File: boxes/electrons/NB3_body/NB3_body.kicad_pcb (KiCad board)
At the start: 2 copper layers, 200 x 199.5 mm, 36 parts, among them J1 Conn_02x05_Counter_Clockwise, J10 Conn_02x03_Top_Bottom, J11 Conn_02x03_Top_Bottom, J12 Conn_02x03_Top_Bottom, J13 JST ZH 6-way Socket, J14 JST ZH 6-way Socket, J2 Conn_02x05_Counter_Clockwise, J3 Conn_02x05_Counter_Clockwise, J4 Conn_02x05_Counter_Clockwise, J5 Conn_02x05_Counter_Clockwise, J6 Conn_02x05_Counter_Clockwise, J7 Conn_02x05_Counter_Clockwise, J8 Conn_02x05_Counter_Clockwise, J9 JST SH 4-way Socket

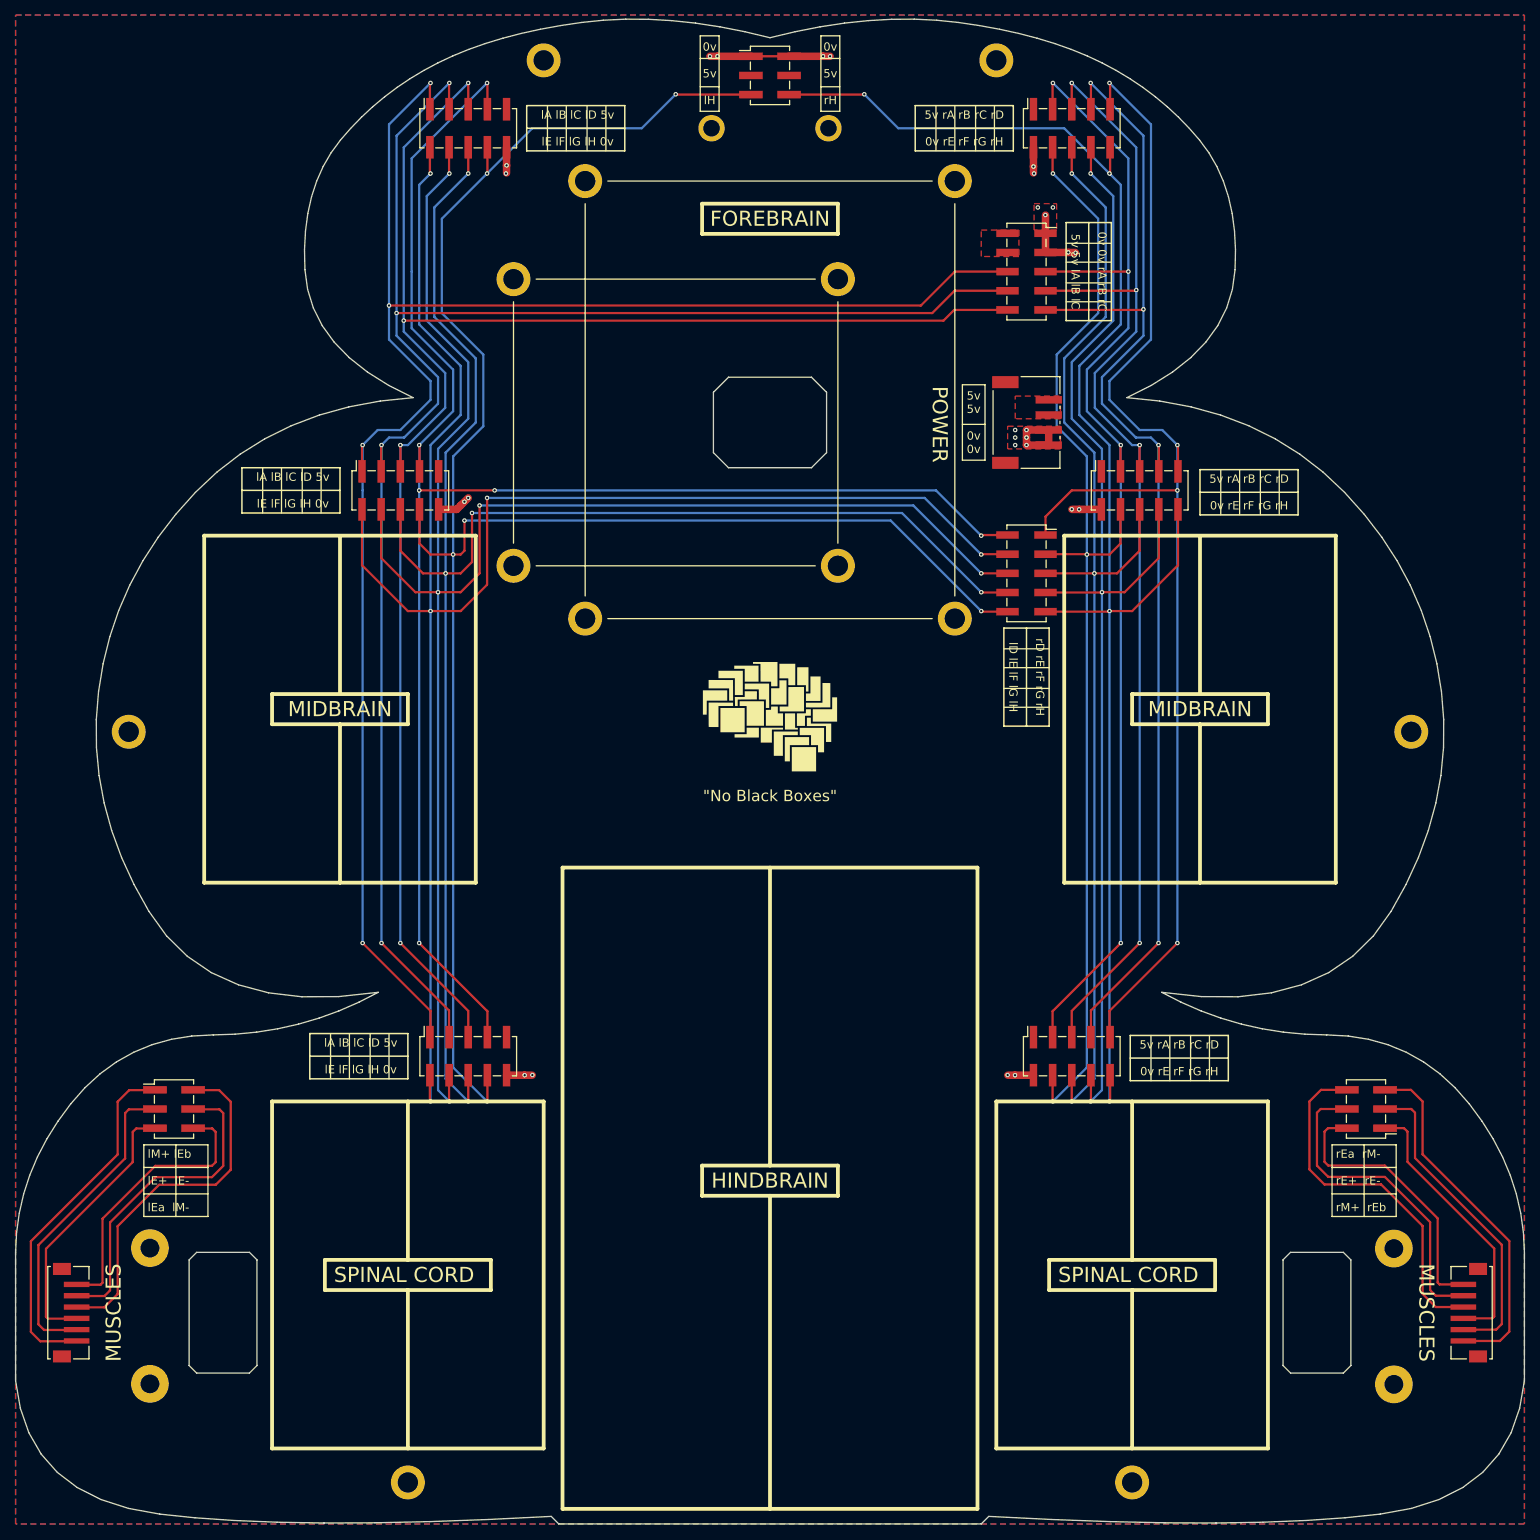
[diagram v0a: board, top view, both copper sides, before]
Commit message: Update NB3_body (motor mount holes)
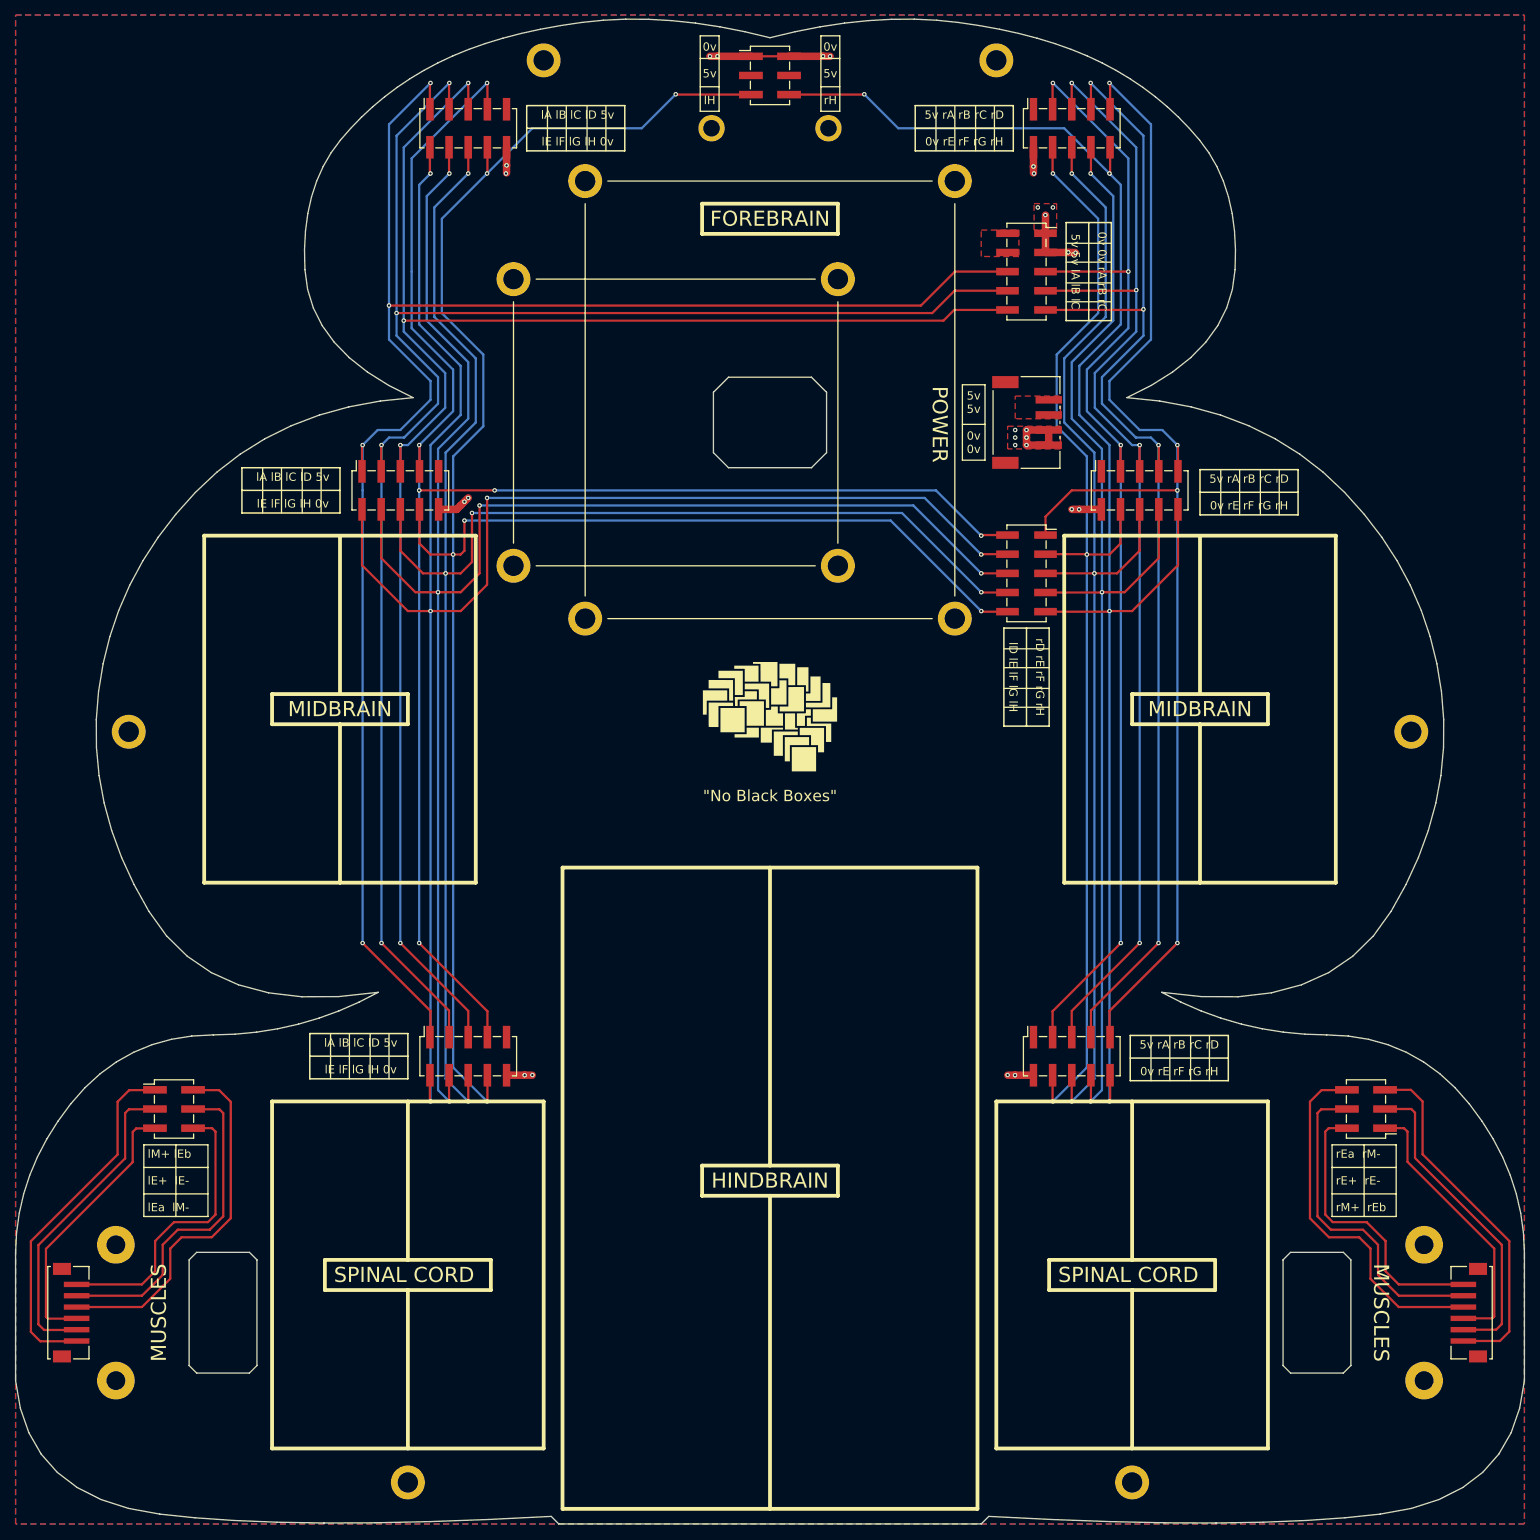
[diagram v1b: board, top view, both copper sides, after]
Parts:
- moved H11 4.53 mm to (37.8, 204.0)
- moved H9 4.53 mm to (37.8, 186.0)
- moved H10 4.03 mm to (211.2, 186.0)
- moved H12 4.03 mm to (211.2, 204.0)
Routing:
- net /LM-: track 37.3 -> 38.7 mm
- net /RM+: track 37.3 -> 38.7 mm
- net /RE+: track 43.0 -> 44.0 mm
- net /LE-: track 43.0 -> 44.0 mm
- net /RE A: track 47.8 -> 48.7 mm
- net /LE B: track 47.8 -> 48.7 mm
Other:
- board text added: "NB3_body Rev 0.0.2"
- board text removed: "NB3_body Rev 0.0.1"

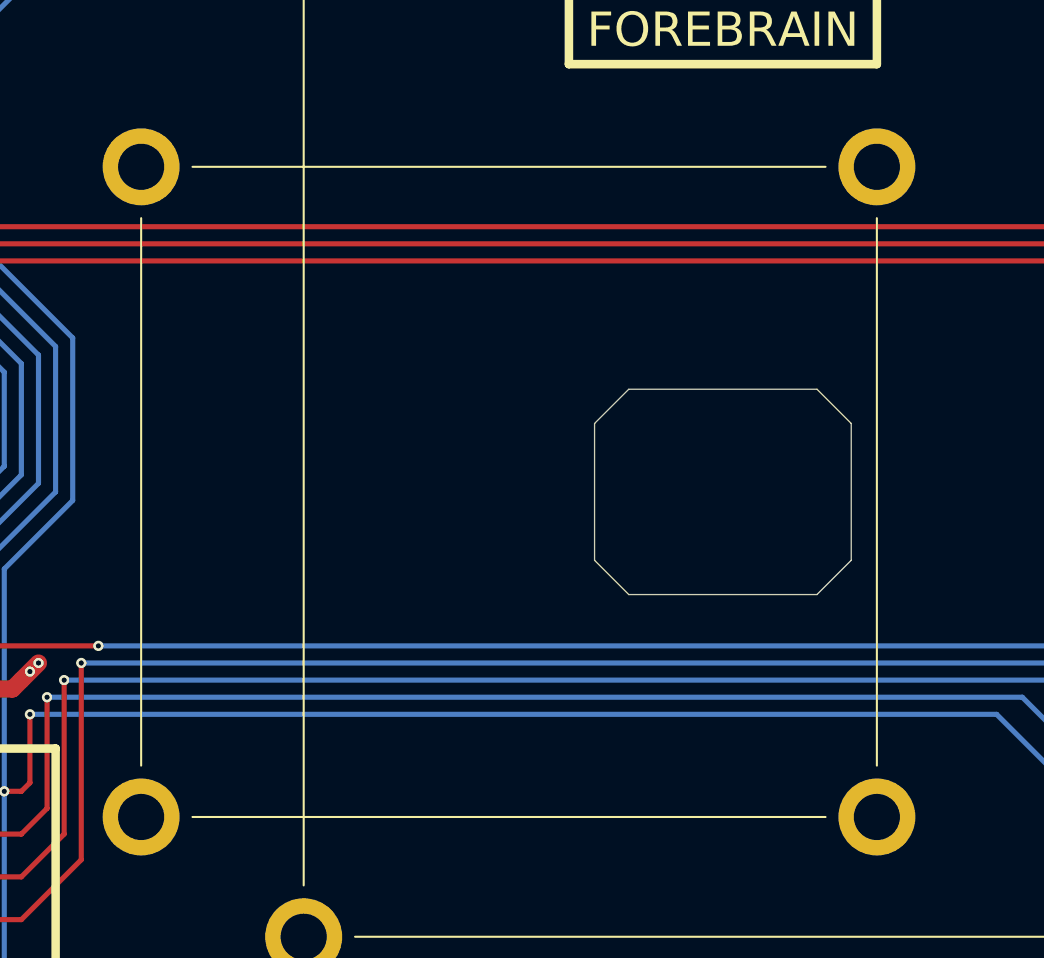
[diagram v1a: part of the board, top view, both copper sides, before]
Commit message: Update NB3_body: new power dimensions
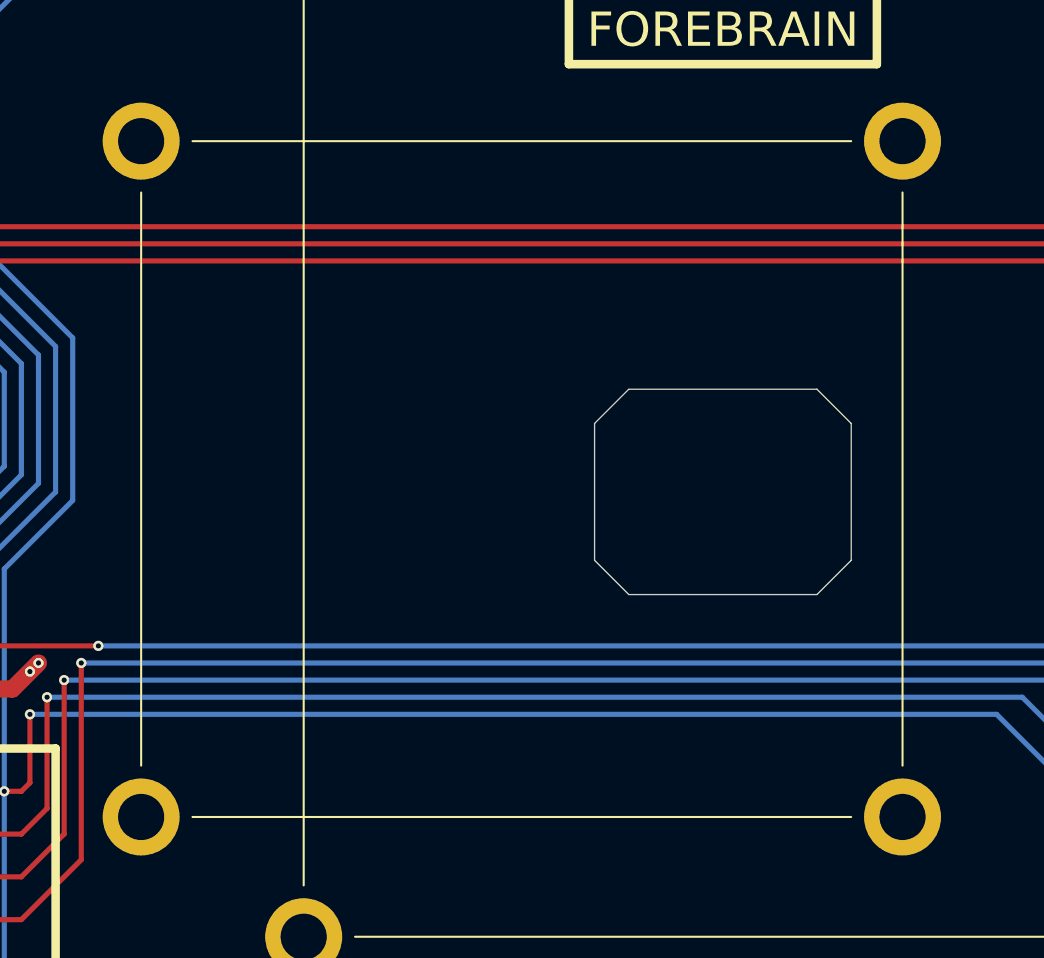
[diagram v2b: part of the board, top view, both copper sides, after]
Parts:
- moved H2 2.12 mm to (135.0, 56.5)
- moved H1 1.50 mm to (90.5, 56.5)
- moved H4 1.50 mm to (135.0, 96.0)
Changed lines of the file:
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@@
   )
   (footprint "MountingHole:MountingHole_2.7mm_M2.5_ISO7380_Pad" (layer "F.Cu")
-    (at 133.5 58)
+    (at 135 56.5)
     (descr "Mounting Hole 2.7mm, M2.5, ISO7380")
     (tags "mounting hole 2.7mm m2.5 iso7380")
@@
   )
   (footprint "MountingHole:MountingHole_2.7mm_M2.5_ISO7380_Pad" (layer "F.Cu")
-    (at 133.5 96)
+    (at 135 96)
     (descr "Mounting Hole 2.7mm, M2.5, ISO7380")
     (tags "mounting hole 2.7mm m2.5 iso7380")
@@
   )
   (footprint "MountingHole:MountingHole_2.7mm_M2.5_ISO7380_Pad" (layer "F.Cu")
-    (at 90.5 58)
+    (at 90.5 56.5)
     (descr "Mounting Hole 2.7mm, M2.5, ISO7380")
     (tags "mounting hole 2.7mm m2.5 iso7380")
@@
   (gr_line (start 68.75 158) (end 68.75 164) (layer "F.SilkS") (width 0.12))
   (gr_line (start 65 83) (end 65 89) (layer "F.SilkS") (width 0.12))
-  (gr_line (start 133.5 61) (end 133.5 93) (layer "F.SilkS") (width 0.12))
+  (gr_line (start 135 59.5) (end 135 93) (layer "F.SilkS") (width 0.12))
   (gr_line (start 115.25 28.75) (end 117.75 28.75) (layer "F.SilkS") (width 0.12))
   (gr_rect (start 41.5 172.75) (end 50 182.25) (layer "F.SilkS") (width 0.12) (fill none))
@@
   (gr_line (start 181.5 117) (end 181.5 138) (layer "F.SilkS") (width 0.5))
   (gr_line (start 105.25 41) (end 105.25 35) (layer "F.SilkS") (width 0.2))
-  (gr_line (start 93.5 58) (end 130.5 58) (layer "F.SilkS") (width 0.12))
-  (gr_line (start 90.5 93) (end 90.5 61) (layer "F.SilkS") (width 0.12))
+  (gr_line (start 93.5 56.5) (end 132 56.5) (layer "F.SilkS") (width 0.12))
+  (gr_line (start 90.5 93) (end 90.5 59.5) (layer "F.SilkS") (width 0.12))
   (gr_line (start 186.75 83.25) (end 186.75 89.25) (layer "F.SilkS") (width 0.12))
   (gr_line (start 166.75 50.5) (end 166.75 63.5) (layer "F.SilkS") (width 0.2))
@@
   (gr_line (start 182.75 158.25) (end 182.75 164.25) (layer "F.SilkS") (width 0.12))
   (gr_line (start 146.5 35) (end 146.5 41) (layer "F.SilkS") (width 0.12))
-  (gr_line (start 130.5 96) (end 93.5 96) (layer "F.SilkS") (width 0.12))
+  (gr_line (start 132 96) (end 93.5 96) (layer "F.SilkS") (width 0.12))
   (gr_line (start 152 136) (end 97 136) (layer "F.SilkS") (width 0.5))
   (gr_line (start 66.25 158) (end 66.25 164) (layer "F.SilkS") (width 0.12))

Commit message: Added new NB3_body fab details
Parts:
- moved H1 0.50 mm to (91.0, 56.5)
- moved H2 0.50 mm to (135.5, 56.5)
- moved H3 0.50 mm to (91.0, 96.0)
- moved H4 0.50 mm to (135.5, 96.0)
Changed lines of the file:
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@@
       (sketchpadsonfab false)
       (subtractmaskfromsilk false)
-      (outputformat 3)
+      (outputformat 1)
       (mirror false)
       (drillshape 0)
       (scaleselection 1)
-      (outputdirectory "fab/")
+      (outputdirectory "fab_2/")
     )
   )
@@
   )
   (footprint "MountingHole:MountingHole_2.7mm_M2.5_ISO7380_Pad" (layer "F.Cu")
-    (at 135 56.5)
+    (at 135.5 56.5)
     (descr "Mounting Hole 2.7mm, M2.5, ISO7380")
     (tags "mounting hole 2.7mm m2.5 iso7380")
@@
   )
   (footprint "MountingHole:MountingHole_2.7mm_M2.5_ISO7380_Pad" (layer "F.Cu")
-    (at 90.5 96)
+    (at 91 96)
     (descr "Mounting Hole 2.7mm, M2.5, ISO7380")
     (tags "mounting hole 2.7mm m2.5 iso7380")
@@
   )
   (footprint "MountingHole:MountingHole_2.7mm_M2.5_ISO7380_Pad" (layer "F.Cu")
-    (at 135 96)
+    (at 135.5 96)
     (descr "Mounting Hole 2.7mm, M2.5, ISO7380")
     (tags "mounting hole 2.7mm m2.5 iso7380")
@@
   )
   (footprint "MountingHole:MountingHole_2.7mm_M2.5_ISO7380_Pad" (layer "F.Cu")
-    (at 90.5 56.5)
+    (at 91 56.5)
     (descr "Mounting Hole 2.7mm, M2.5, ISO7380")
     (tags "mounting hole 2.7mm m2.5 iso7380")
@@
   (gr_line (start 68.75 158) (end 68.75 164) (layer "F.SilkS") (width 0.12))
   (gr_line (start 65 83) (end 65 89) (layer "F.SilkS") (width 0.12))
-  (gr_line (start 135 59.5) (end 135 93) (layer "F.SilkS") (width 0.12))
+  (gr_line (start 135.5 59.5) (end 135.5 93) (layer "F.SilkS") (width 0.12))
   (gr_line (start 115.25 28.75) (end 117.75 28.75) (layer "F.SilkS") (width 0.12))
   (gr_rect (start 41.5 172.75) (end 50 182.25) (layer "F.SilkS") (width 0.12) (fill none))
@@
   (gr_line (start 181.5 117) (end 181.5 138) (layer "F.SilkS") (width 0.5))
   (gr_line (start 105.25 41) (end 105.25 35) (layer "F.SilkS") (width 0.2))
-  (gr_line (start 93.5 56.5) (end 132 56.5) (layer "F.SilkS") (width 0.12))
-  (gr_line (start 90.5 93) (end 90.5 59.5) (layer "F.SilkS") (width 0.12))
+  (gr_line (start 94 56.5) (end 132.5 56.5) (layer "F.SilkS") (width 0.12))
+  (gr_line (start 91 93) (end 91 59.5) (layer "F.SilkS") (width 0.12))
   (gr_line (start 186.75 83.25) (end 186.75 89.25) (layer "F.SilkS") (width 0.12))
   (gr_line (start 166.75 50.5) (end 166.75 63.5) (layer "F.SilkS") (width 0.2))
@@
   (gr_line (start 182.75 158.25) (end 182.75 164.25) (layer "F.SilkS") (width 0.12))
   (gr_line (start 146.5 35) (end 146.5 41) (layer "F.SilkS") (width 0.12))
-  (gr_line (start 132 96) (end 93.5 96) (layer "F.SilkS") (width 0.12))
+  (gr_line (start 132.5 96) (end 94 96) (layer "F.SilkS") (width 0.12))
   (gr_line (start 152 136) (end 97 136) (layer "F.SilkS") (width 0.5))
   (gr_line (start 66.25 158) (end 66.25 164) (layer "F.SilkS") (width 0.12))
